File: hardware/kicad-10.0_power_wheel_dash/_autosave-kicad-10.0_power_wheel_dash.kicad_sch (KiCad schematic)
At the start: 24 parts, among them J1 LCD_Module, J2 MicroSD_Module, J3 Bat 24V, U1 ESP32-S3-WROOM-1, U2 MAX98357A Module, U3 SN74AHCT125N, U4 MP1584EN Module, U5 MP1584EN Module

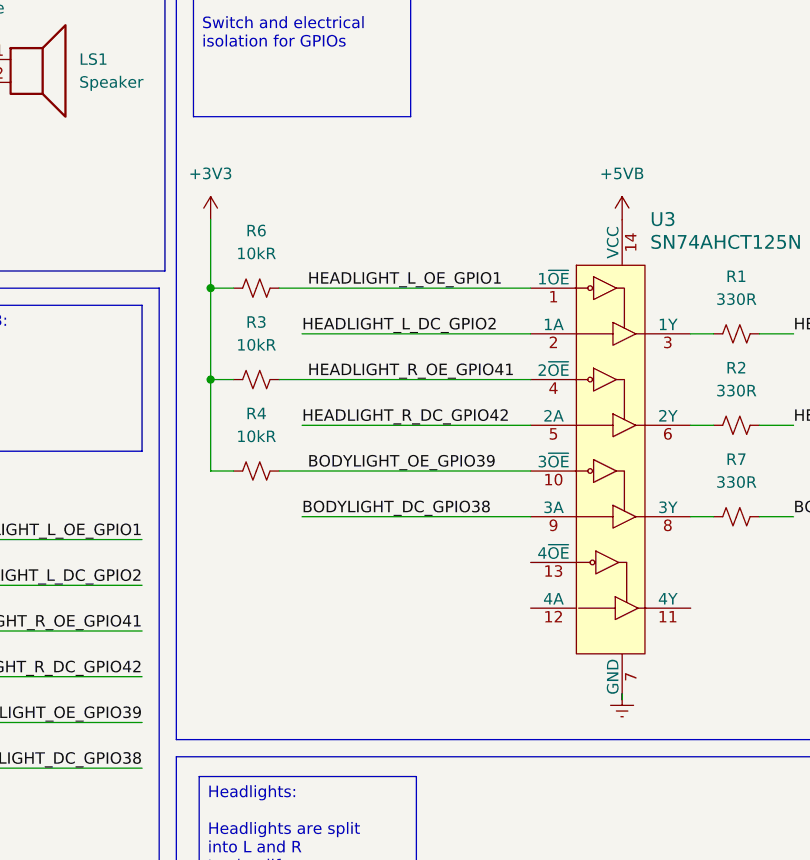
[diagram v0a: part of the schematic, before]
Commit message: sorting out thread safety and architecture around lvgl
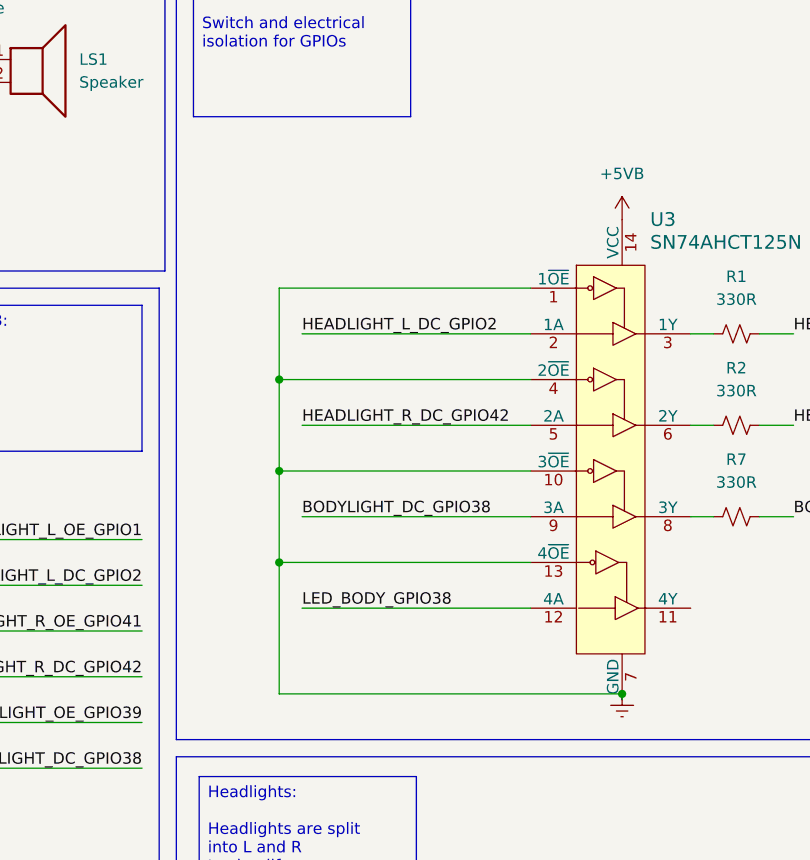
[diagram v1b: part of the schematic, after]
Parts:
- removed R3, R4, R6: 10kR, symbol Device:R_Small_US
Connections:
- net BODYLIGHT_OE_GPIO39: no longer U3.10 (3~{OE})
- net GNDREF: now also U3.1 (1~{OE}), U3.10 (3~{OE}), U3.13 (4~{OE}), U3.4 (2~{OE})
- net HEADLIGHT_L_OE_GPIO1: no longer U3.1 (1~{OE})
- net HEADLIGHT_R_OE_GPIO41: no longer U3.4 (2~{OE})
- net LED_BODY_GPIO38: now reaches U3.12 (4A)
